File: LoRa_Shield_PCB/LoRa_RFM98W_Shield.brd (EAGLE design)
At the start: 53.6 x 59.9 mm, 40 parts, among them IC1 AHT10, IC2 TXS0102DCUR, J1 TYPE-C-31-M-17, J2 CON_TERMINAL_BLOCK_03-5MM, U1 3V3_REG, U2 RFM98W, X1 BU-SMA-H

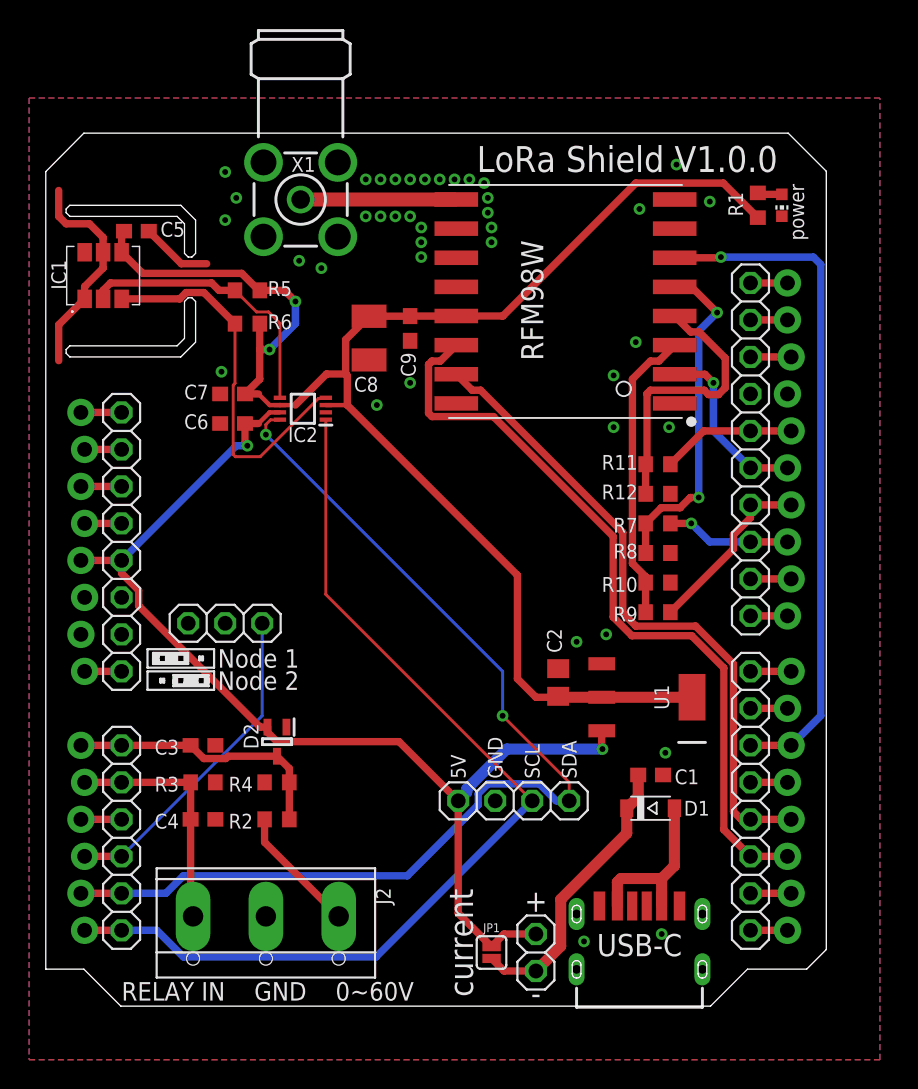
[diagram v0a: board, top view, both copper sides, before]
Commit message: parts updated for LCSC orders
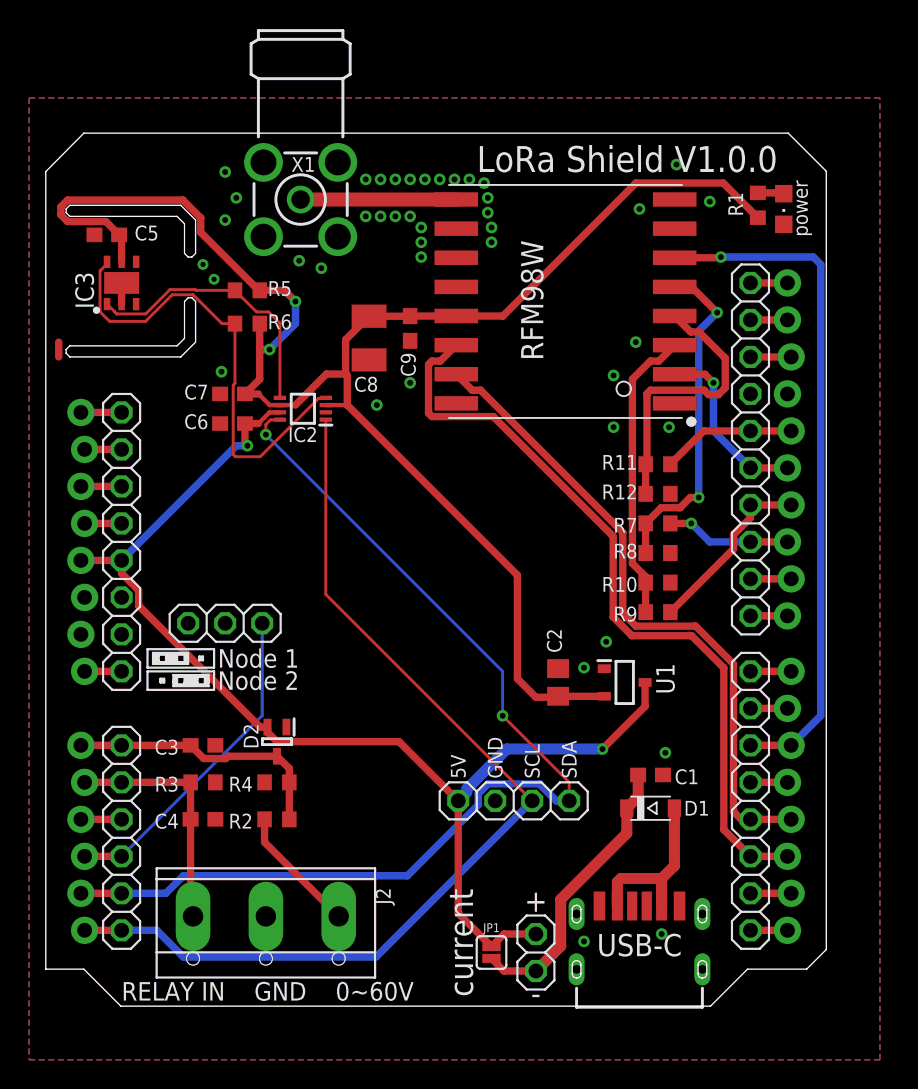
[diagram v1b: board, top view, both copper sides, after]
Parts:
- removed IC1: AHT10, SamacSys_Parts:AHT10
- added IC3: SHT20, SamacSys_Parts:SON100P300X300X110-7N
- LED1: value green -> (none); device adafruit:CHIP-LED0603 -> led:CHIPLED_0805
- U1: value 3V3_REG -> XC6206P332MR; device SamacSys_Parts:SOT230P700X170-4N -> SamacSys_Parts:SOT95P280X130-3N
- moved C5 2.05 mm to (7.87, 56.6), turned to 0 degrees
- moved U1 1.83 mm to (43.4, 25.9), turned to 0 degrees
- moved LED1 0.28 mm to (54.4, 58.4)
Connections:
- net 3.3V: now also IC3.5; no longer IC1.4, U1.4
- net GND: now also IC3.2, IC3.7; no longer IC1.1, IC1.5
- net I2C_SCL_3V3: now also IC3.6; no longer IC1.3
- net I2C_SDA_3V3: now also IC3.1; no longer IC1.2
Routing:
- net GND: track 20.0 -> 2.47 mm, vias 40 -> 42
- net 3.3V: track 108.9 -> 114.9 mm
- net I2C_SCL_3V3: track 26.0 -> 31.9 mm
- net 5V: track 77.4 -> 82.0 mm

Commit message: PCB production V1.0.0
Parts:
- renumbered IC3 to IC1
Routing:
- net GND: track 2.47 -> 1.45 mm
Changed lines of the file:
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@@
 <attribute name="NAME" x="46.228" y="26.162" size="1.27" layer="25" rot="R90" align="center"/>
 </element>
-<element name="IC3" library="SamacSys_Parts" package="SON100P300X300X110-7N" value="SHT20" x="8.89" y="53.34" smashed="yes" rot="R90">
+<element name="IC1" library="SamacSys_Parts" package="SON100P300X300X110-7N" value="SHT20" x="8.89" y="53.34" smashed="yes" rot="R90">
 <attribute name="DESCRIPTION" value="Sensirion SHT20, Temperature &amp; Humidity Sensor -40  +125 C +/-3 (Humidity) %RH, +/-3 (Temperature) C" x="8.89" y="53.34" size="1.778" layer="27" rot="R90" display="off"/>
 <attribute name="HEIGHT" value="1.1mm" x="8.89" y="53.34" size="1.778" layer="27" rot="R90" display="off"/>
@@
 <contactref element="LED1" pad="C"/>
 <contactref element="U1" pad="1"/>
-<contactref element="IC3" pad="2"/>
-<wire x1="4.572" y1="49.276" x2="4.572" y2="48.26" width="0.508" layer="1"/>
-<contactref element="IC3" pad="7"/>
+<contactref element="IC1" pad="2"/>
+<contactref element="IC1" pad="7"/>
 <wire x1="8.89" y1="51.89" x2="8.89" y2="53.34" width="0.508" layer="1"/>
 <via x="15.24" y="53.594" extent="1-16" drill="0.35"/>
@@
 <wire x1="34.29" y1="7.7724" x2="32.004" y2="10.0584" width="0.508" layer="1"/>
 <via x="41.91" y="21.336" extent="1-16" drill="0.4"/>
-<wire x1="41.91" y1="21.336" x2="41.858" y2="21.388" width="0.508" layer="1"/>
 <contactref element="U1" pad="3"/>
 <wire x1="41.91" y1="21.336" x2="44.834" y2="24.26" width="0.508" layer="1"/>
@@
 <wire x1="37.338" y1="24.892" x2="38.796" y2="24.892" width="0.508" layer="1"/>
 <wire x1="38.796" y1="24.892" x2="38.862" y2="24.958" width="0.508" layer="1"/>
-<wire x1="38.928" y1="24.892" x2="38.862" y2="24.958" width="0.508" layer="1"/>
 <contactref element="U1" pad="2"/>
 <wire x1="38.862" y1="24.958" x2="42.034" y2="24.958" width="0.508" layer="1"/>
-<contactref element="IC3" pad="5"/>
+<contactref element="IC1" pad="5"/>
 <wire x1="5.1867" y1="57.5564" x2="4.7244" y2="58.0187" width="0.508" layer="1"/>
 <wire x1="4.7244" y1="58.0187" x2="4.7244" y2="58.5673" width="0.508" layer="1"/>
@@
 <wire x1="18.9812125" y1="51.35" x2="19.761" y2="50.5702125" width="0.2032" layer="1"/>
 <wire x1="19.761" y1="50.5702125" x2="19.761" y2="45.454" width="0.2032" layer="1"/>
-<contactref element="IC3" pad="1"/>
+<contactref element="IC1" pad="1"/>
 <wire x1="8.411" y1="51.3597875" x2="8.5597875" y2="51.211" width="0.2032" layer="1"/>
 <wire x1="12.21453125" y1="52.8828" x2="13.94746875" y2="52.8828" width="0.2032" layer="1"/>
@@
 <wire x1="22.403" y1="45.4077875" x2="18.4052125" y2="41.41" width="0.2032" layer="1"/>
 <wire x1="16.556" y1="46.3252125" x2="16.556" y2="41.5587875" width="0.2032" layer="1"/>
-<contactref element="IC3" pad="6"/>
+<contactref element="IC1" pad="6"/>
 <wire x1="7.411" y1="51.3597875" x2="8.067784375" y2="50.703003125" width="0.2032" layer="1"/>
 <wire x1="12.36183125" y1="52.5272" x2="13.80016875" y2="52.5272" width="0.2032" layer="1"/>

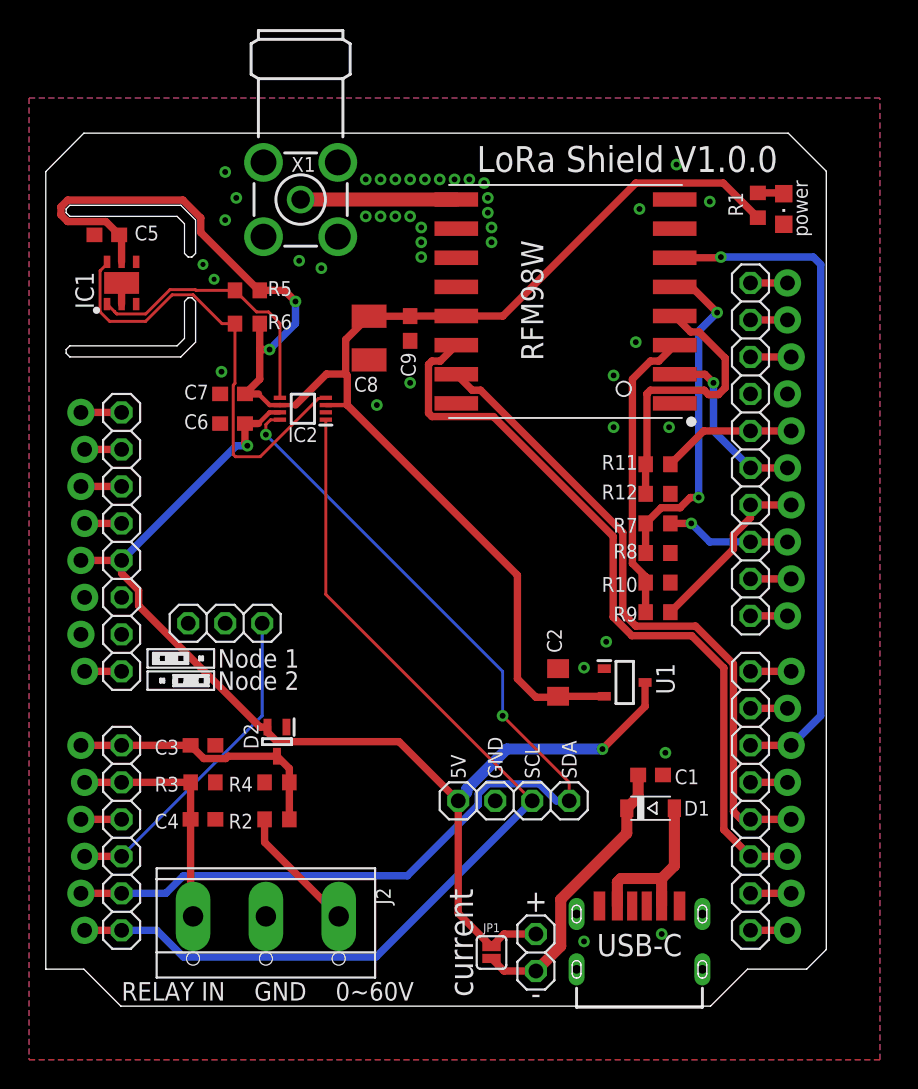
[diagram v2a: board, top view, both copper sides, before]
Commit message: fixed copper pour, OLED orientation problem, optimized layout
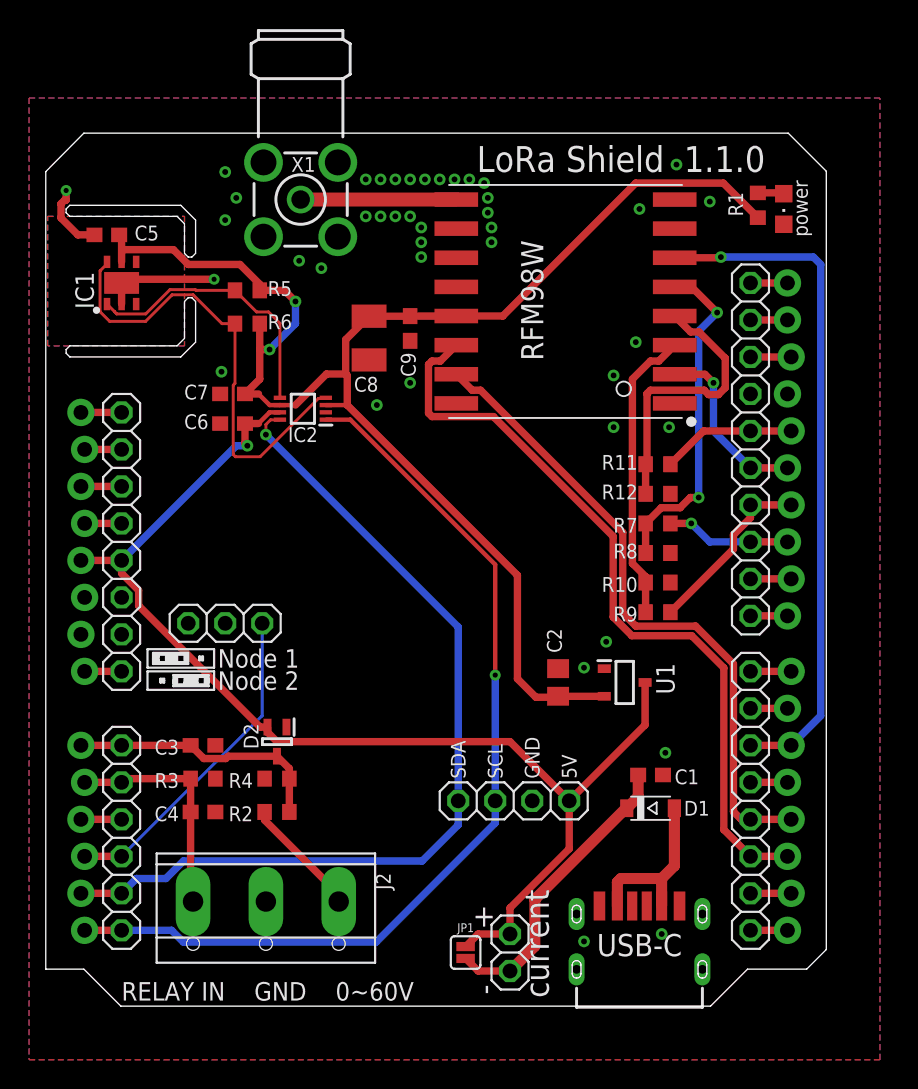
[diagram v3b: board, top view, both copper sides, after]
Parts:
- moved JP1 1.78 mm to (32.5, 7.37)
- moved JP2 1.78 mm to (35.6, 7.37)
- moved J2 1.02 mm to (18.8, 10.4)
- moved C4 0.51 mm to (14.5, 17.0)
- moved R2 0.51 mm to (19.6, 17.0)
- moved R3 0.25 mm to (14.5, 19.3)
- moved R4 0.25 mm to (19.6, 19.3)
- turned JP3 to 180 degrees
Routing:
- net GND: track 1.45 -> 12.9 mm
- net I2C_SDA_5V: track 73.1 -> 61.9 mm, vias 2 -> 1
- net 3.3V: track 114.8 -> 103.7 mm
- net I2C_SCL_5V: track 68.0 -> 65.4 mm, vias 0 -> 1
- net N$16: track 19.8 -> 20.5 mm
- net INPUT_RELAY_STATUS: track 16.5 -> 15.9 mm
- net N$8: track 8.77 -> 8.26 mm
- net INPUT_VOLTAGE_READING: track 18.6 -> 18.1 mm
- net 5V: track 81.9 -> 82.4 mm, vias 2 -> 1
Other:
- board text added: ">CREVISION"
- board text added: "LoRa Shield"
- board text removed: "LoRa Shield V1.0.0"

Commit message: schematic resistor value, arduino code
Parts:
- R2: value 165k -> 110k
- R4: value 15k -> 10k
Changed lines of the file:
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@@
 <attribute name="SPICEPREFIX" value="R" x="14.478" y="12.954" size="1.4224" layer="27" ratio="12" rot="R180" display="off"/>
 </element>
-<element name="R2" library="rcl" library_urn="urn:adsk.eagle:library:334" package="R0603" package3d_urn="urn:adsk.eagle:package:23555/3" value="165k" x="19.558" y="17.018" smashed="yes" rot="R180">
+<element name="R2" library="rcl" library_urn="urn:adsk.eagle:library:334" package="R0603" package3d_urn="urn:adsk.eagle:package:23555/3" value="110k" x="19.558" y="17.018" smashed="yes" rot="R180">
 <attribute name="NAME" x="17.907" y="17.399" size="1.016" layer="25" ratio="12" rot="R180"/>
 <attribute name="POPULARITY" value="77" x="34.29" y="21.844" size="1.4224" layer="27" ratio="12" rot="R180" display="off"/>
 <attribute name="SPICEPREFIX" value="R" x="34.29" y="21.844" size="1.4224" layer="27" ratio="12" rot="R180" display="off"/>
 </element>
-<element name="R4" library="rcl" library_urn="urn:adsk.eagle:library:334" package="R0603" package3d_urn="urn:adsk.eagle:package:23555/3" value="15k" x="19.558" y="19.304" smashed="yes">
+<element name="R4" library="rcl" library_urn="urn:adsk.eagle:library:334" package="R0603" package3d_urn="urn:adsk.eagle:package:23555/3" value="10k" x="19.558" y="19.304" smashed="yes">
 <attribute name="NAME" x="17.907" y="19.685" size="1.016" layer="25" ratio="12" rot="R180"/>
 <attribute name="POPULARITY" value="77" x="15.24" y="15.494" size="1.4224" layer="27" ratio="12" display="off"/>
